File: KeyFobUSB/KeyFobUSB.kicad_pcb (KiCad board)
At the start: 2 copper layers, 54.3 x 18 mm, 17 parts, among them J1 USB_A, SW2 SW_SPDT, U1 ATtiny85V-10S

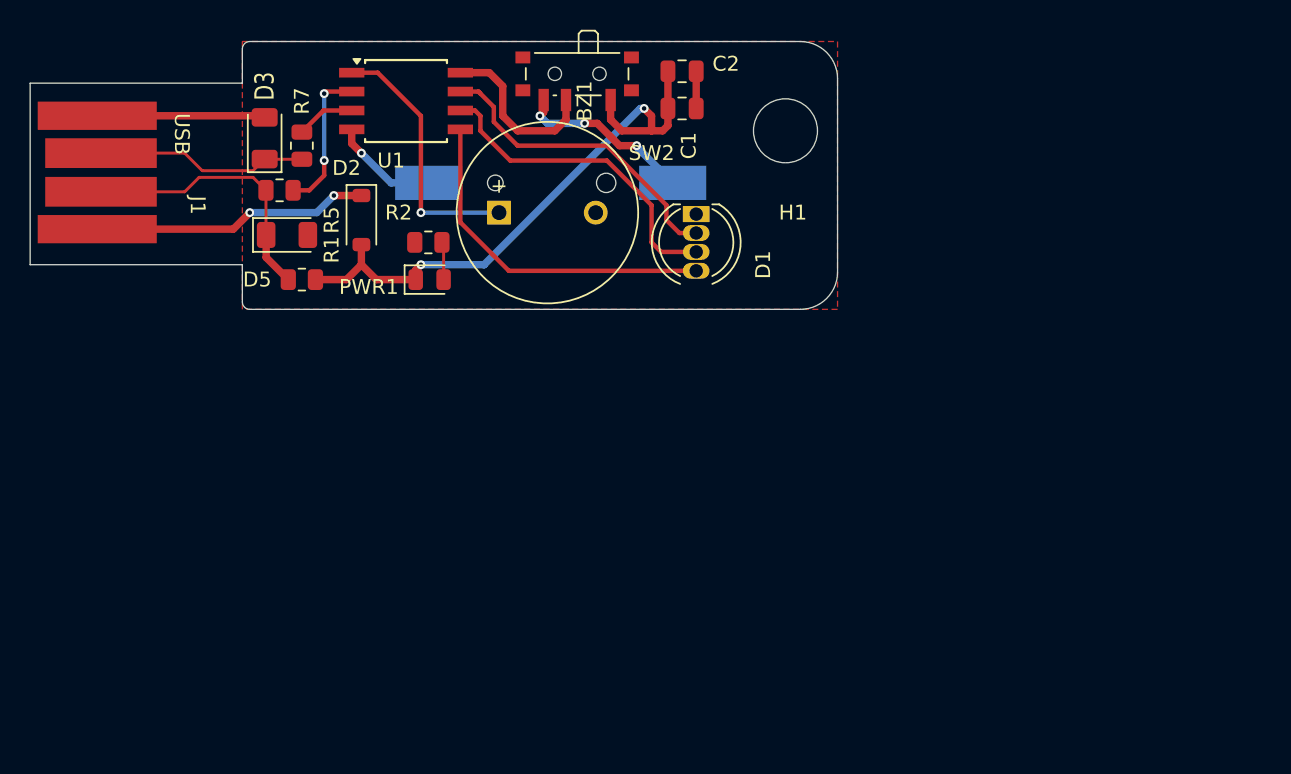
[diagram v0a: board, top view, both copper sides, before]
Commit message: Completed the schematic and placed the components on pcb
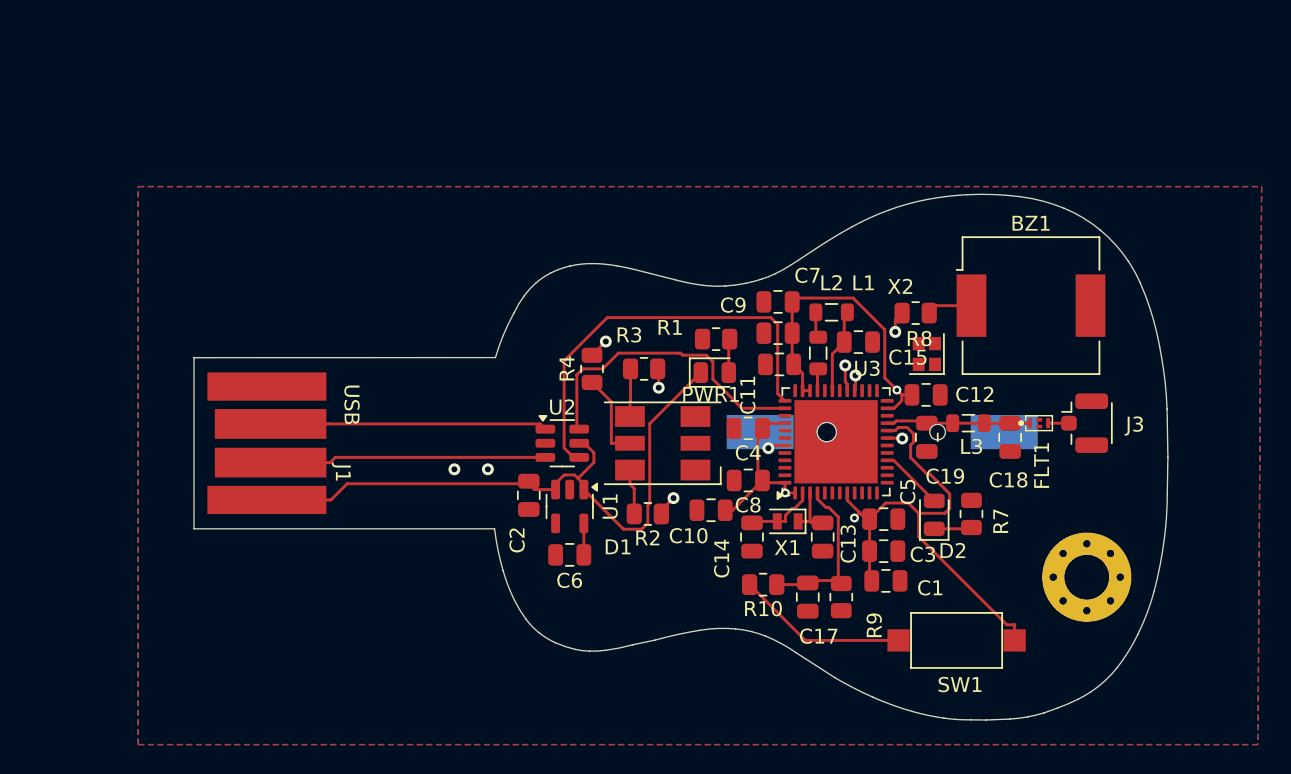
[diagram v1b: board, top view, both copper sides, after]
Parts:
- removed BT1: Battery_Cell, 22BatteryHoldercoincell_S8411-45R:S8411-45R_1
- removed D3, D5: 3.6V, Diode_SMD:D_1206_3216Metric
- removed H1: MountingHole, MountingHole:MountingHole_4.3mm_M4
- removed R5: 68, Resistor_SMD:R_0805_2012Metric
- removed SW2: SW_SPDT, Button_Switch_SMD:SW_SPDT_PCM12
- added C10: 100n, Capacitor_SMD:C_0805_2012Metric, F.Cu at (133.5, 79.5)
- added C11: 100n, Capacitor_SMD:C_0805_2012Metric, F.Cu at (138.1, 69.7)
- added C12: 100n, Capacitor_SMD:C_0805_2012Metric, F.Cu at (147.9, 71.8)
- added C13: 10p, Capacitor_SMD:C_0805_2012Metric, F.Cu at (141.0, 81.3)
- added C14: 10p, Capacitor_SMD:C_0805_2012Metric, F.Cu at (136.2, 81.3)
- added C15: 4u7, Capacitor_SMD:C_0805_2012Metric, F.Cu at (143.4, 68.2)
- added C17: 100n, Capacitor_SMD:C_0805_2012Metric, F.Cu at (140.0, 85.3)
- added C18: 0p8, Capacitor_SMD:C_0805_2012Metric, F.Cu at (153.6, 74.6)
- added C19: 0p8, Capacitor_SMD:C_0805_2012Metric, F.Cu at (148.0, 74.6)
- added C3: 100n, Capacitor_SMD:C_0805_2012Metric, F.Cu at (145.1, 82.2)
- added C4: 100n, Capacitor_SMD:C_0805_2012Metric, F.Cu at (136.0, 74.0)
- added C5: 100n, Capacitor_SMD:C_0805_2012Metric, F.Cu at (145.1, 80.1)
- added C6: 4u7, Capacitor_SMD:C_0805_2012Metric, F.Cu at (124.0, 82.5)
- added C7: 100n, Capacitor_SMD:C_0805_2012Metric, F.Cu at (138.0, 67.6)
- added C8: 100n, Capacitor_SMD:C_0805_2012Metric, F.Cu at (136.0, 77.5)
- added C9: 4u7, Capacitor_SMD:C_0805_2012Metric, F.Cu at (138.0, 65.5)
- added FLT1: DLF162500LT-5028A1, DLF162500LT-5028A1:DLF162500LT-5028A1, F.Cu at (155.5, 73.7)
- added H+1: MountingHole_Pad, MountingHole:MountingHole_3mm_Pad_Via, F.Cu at (158.8, 84.0)
- added J2: S8411-45R, 22BatteryHoldercoincell_S8411-45R:S8411-45R_1, B.Cu at (145.0, 74.2)
- added J3: Conn_Coaxial, Connector_Coaxial:U.FL_Hirose_U.FL-R-SMT-1_Vertical, F.Cu at (158.6, 73.7)
- added L1: 10n, Inductor_SMD:L_0805_2012Metric, F.Cu at (140.7, 68.9)
- added L2: 10u, Inductor_SMD:L_0805_2012Metric, F.Cu at (141.6, 66.2)
- added L3: 2n7, Inductor_SMD:L_0805_2012Metric, F.Cu at (150.8, 73.7)
- added R10: 220, Resistor_SMD:R_0805_2012Metric, F.Cu at (137.0, 84.5)
- added R3: 220, Resistor_SMD:R_0805_2012Metric, F.Cu at (129.0, 70.0)
- added R4: 220, Resistor_SMD:R_0805_2012Metric, F.Cu at (125.5, 70.0)
- added R8: 220, Resistor_SMD:R_0805_2012Metric, F.Cu at (147.2, 66.2)
- added R9: 5k1, Resistor_SMD:R_0805_2012Metric, F.Cu at (142.2, 85.3)
- added SW1: SW_Push, Button_Switch_SMD:SW_SPST_CK_RS282G05A3, F.Cu at (150.0, 88.2)
- added U2: USBLC6-2SC6, Package_TO_SOT_SMD:SOT-23-6, F.Cu at (123.5, 75.0)
- added U3: STM32WB55CEU6, Package_DFN_QFN:QFN-48-1EP_7x7mm_P0.5mm_EP5.6x5.6mm, F.Cu at (141.9, 74.9)
- added X1: 32kHz768, Crystal:Crystal_SMD_2012-2Pin_2.0x1.2mm, F.Cu at (138.7, 80.2)
- added X2: 32MHz, Crystal:Crystal_SMD_2016-4Pin_2.0x1.6mm, F.Cu at (148.0, 69.0)
- BZ1: footprint Buzzer_Beeper:MagneticBuzzer_ProSignal_ABT-410-RC -> Buzzer_Beeper:Buzzer_CUI_CPT-9019S-SMT
- C1: value 4.7uF -> 4u7
- C2: value 0.1uF -> 4u7
- D1: value LED_KRGB -> LED_RGB; footprint LED_THT:LED_D5.0mm-4_RGB -> LED_SMD:LED_Inolux_IN-P55TATRGB_PLCC6_5.0x5.5mm_P1.8mm
- D2: value MBR0520LT -> LED; footprint Diode_SMD:D_SOD-123 -> LED_SMD:LED_0805_2012Metric
- R1: value 1K5 -> 1K
- R2: value 1K -> 220
- R7: value 68 -> 220
- U1: value ATtiny85V-10S -> MIC5365-3.3YD5; footprint Package_SO:SOIC-8W_5.3x5.3mm_P1.27mm -> Package_TO_SOT_SMD:SOT-23-5
- moved R7 51.4 mm to (151.0, 79.8)
- moved D2 43.3 mm to (148.5, 79.8), turned to 90 degrees
- moved BZ1 36.3 mm to (155.0, 65.8)
- moved C1 34.6 mm to (145.2, 84.2)
- moved C2 30.3 mm to (121.2, 78.5), turned to -90 degrees
- moved U1 29.4 mm to (124.0, 79.2), turned to -90 degrees
- moved R1 28.1 mm to (133.8, 68.0)
- moved R2 23.5 mm to (129.2, 79.8)
- moved J1 21.5 mm to (98.8, 75.0)
- moved PWR1 20.2 mm to (133.8, 70.2)
- moved D1 15.6 mm to (130.2, 75.0), turned to 180 degrees
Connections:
- BZ1 pad 1: /Buzzer -> Net-(BZ1-+)
- C1 pad 1: +5V -> +3.3V
- D1 pad 2: /Red -> GND
- D1 pad 3: /Green -> GND
- D1 pad 4: /Blue -> Net-(D1-BA)
- D2 pad 1: Net-(D2-K) -> /LED_K
- D2 pad 2: +5V -> /LED_A
- J1 pad 1: Net-(D2-K) -> +5V
- J1 pad 2: /D- -> Net-(J1-D-)
- J1 pad 3: /D+ -> Net-(J1-D+)
- R1 pad 1: +5V -> Net-(PWR1-A)
- R1 pad 2: /D- -> GND
- R2 pad 1: Net-(PWR1-A) -> Net-(U3-PB0)
- R2 pad 2: GND -> Net-(D1-RA)
- R7 pad 1: /PB4 -> GND
- R7 pad 2: /D+ -> /LED_K
- U1 pad 1: /Buzzer -> +5V
- U1 pad 2: /PB3 -> GND
- U1 pad 3: /PB4 -> +5V
- U1 pad 4: GND -> unconnected-(U1-NC-Pad4)
- U1 pad 5: /Blue -> Net-(U1-VOUT)
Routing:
- net +3.3V: track 0.00 -> 80.3 mm, vias 0 -> 3
- net /USB_D-: track 0.00 -> 28.2 mm
- net /Blue: track 23.4 -> 0.00 mm
- net /Green: track 21.8 -> 0.00 mm
- net GND: track 21.5 -> 0.00 mm, vias 1 -> 2
- net /Red: track 21.1 -> 0.00 mm
- net /USB_D+: track 0.00 -> 20.5 mm
- net Net-(U3-PB2): track 0.00 -> 20.1 mm, vias 0 -> 2
- net Net-(U3-PB1): track 0.00 -> 19.8 mm, vias 0 -> 2
- net Net-(D2-K): track 18.7 -> 0.00 mm, vias 2 -> 0
- net Net-(J1-D-): track 0.00 -> 18.6 mm
- net Net-(J1-D+): track 0.00 -> 18.6 mm
- net /D-: track 18.5 -> 0.00 mm
- net Net-(U3-PB0): track 0.00 -> 18.1 mm, vias 0 -> 2
- net /Buzzer: track 17.6 -> 0.00 mm, vias 1 -> 0
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- added copper zone on B.Cu, net GND
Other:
- board size 54.3 x 18 mm -> 65.5 x 35.3 mm
- copper layers 2 -> 4
- rule pad_to_mask_clearance: 0 -> 0.08

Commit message: added battery holder and vias
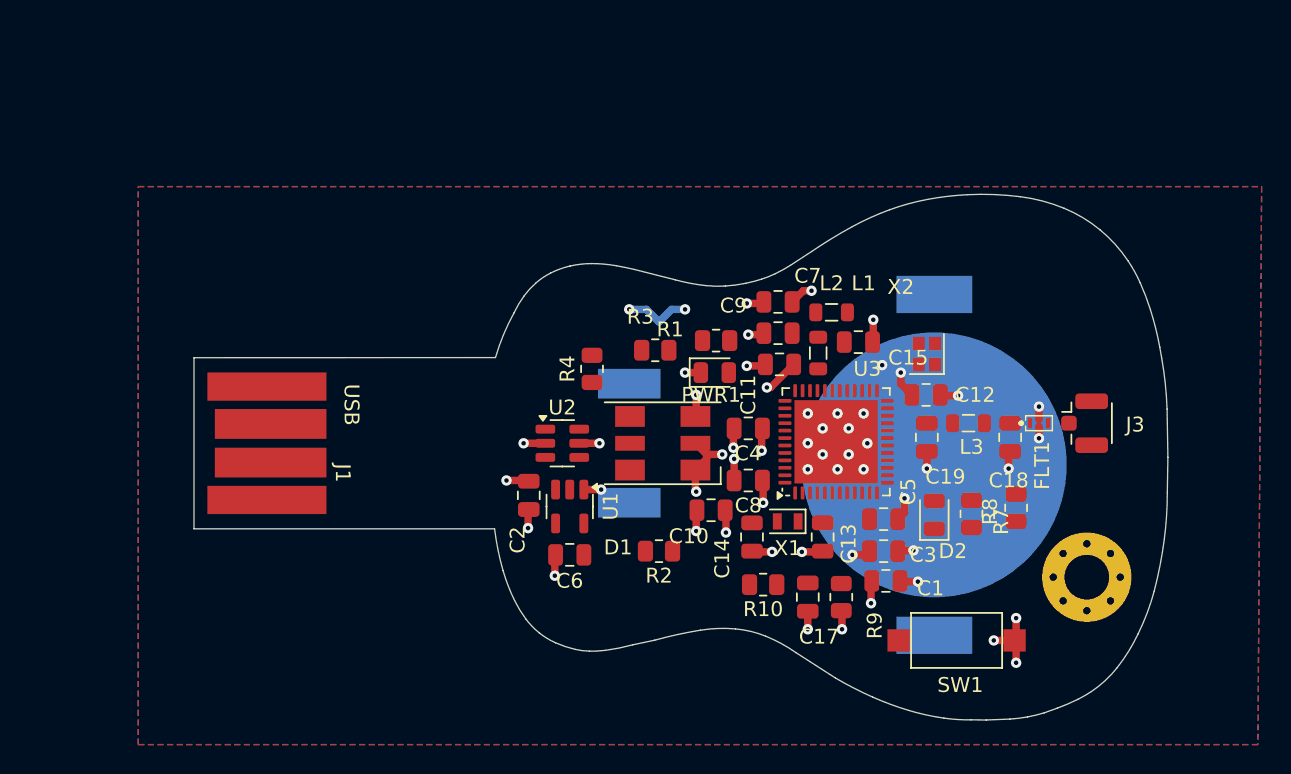
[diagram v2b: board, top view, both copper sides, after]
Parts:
- removed J2: S8411-45R, 22BatteryHoldercoincell_S8411-45R:S8411-45R_1
- added BT1: BAT-HLD-001, 22BatteryHoldercoincell_S8411-45R:BATHLD001 CR2032, B.Cu at (148.5, 76.5)
- BZ1: moved to B.Cu
- moved BZ1 28.5 mm to (128.0, 75.0), turned to 90 degrees
- moved R8 14.7 mm to (154.0, 79.3), turned to 90 degrees
- moved R2 2.61 mm to (130.0, 82.2)
- moved R3 1.46 mm to (129.8, 68.8)
- moved R1 0.10 mm to (133.8, 68.1)
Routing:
- net +3.3V: track 80.3 -> 17.7 mm, vias 3 -> 11
- net GND: track 0.00 -> 42.2 mm, vias 2 -> 40
- net +5V: track 43.9 -> 5.11 mm, vias 0 -> 4
- net /USB_D-: track 28.2 -> 0.00 mm
- net /USB_D+: track 20.5 -> 0.00 mm
- net Net-(U3-PB2): track 20.1 -> 0.00 mm, vias 2 -> 0
- net Net-(U3-PB1): track 19.8 -> 0.00 mm, vias 2 -> 0
- net Net-(J1-D-): track 18.6 -> 0.00 mm
- net Net-(J1-D+): track 18.6 -> 0.00 mm
- net Net-(U3-PB0): track 18.1 -> 0.00 mm, vias 2 -> 0
- net Net-(U3-PB3): track 15.1 -> 0.00 mm, vias 2 -> 0
- net Net-(R10-Pad2): track 11.6 -> 0.00 mm
- net /BOOT0: track 11.1 -> 0.00 mm
- net /RF: track 9.71 -> 0.00 mm
- net Net-(D1-GA): track 5.88 -> 0.00 mm
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- added copper zone on In1.Cu, net GND
- added copper zone on In2.Cu, net GND

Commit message: Added the PCB image
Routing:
- net GND: track 42.2 -> 37.8 mm, vias 40 -> 38
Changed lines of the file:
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@@
 		(layer "Edge.Cuts")
-	)
-	(dimension
-		(type aligned)
-		(layer "B.Cu")
-		(pts
-			(xy 160 65) (xy 160 78)
-		)
-		(height -18)
-		(gr_text "0.5118 in"
-			(at 176.2 71.5 90)
-			(layer "B.Cu")
-			(effects
-				(font
-					(size 1.5 1.5)
-					(thickness 0.3)
-				)
-			)
-		)
-		(format
-			(prefix "")
-			(suffix "")
-			(units 3)
-			(units_format 1)
-			(precision 4)
-		)
-		(style
-			(thickness 0.2)
-			(arrow_length 1.27)
-			(text_position_mode 0)
-			(extension_height 0.58642)
-			(extension_offset 0.5) keep_text_aligned)
 	)
 	(segment
@@
 	)
 	(via
-		(at 131.75 66)
-		(size 0.7)
-		(drill 0.3)
-		(layers "F.Cu" "B.Cu")
-		(free yes)
-		(net 2)
-	)
-	(via
 		(at 139.6 82.3)
 		(size 0.7)
@@
 	(via
 		(at 155.5375 72.5375)
-		(size 0.7)
-		(drill 0.3)
-		(layers "F.Cu" "B.Cu")
-		(free yes)
-		(net 2)
-	)
-	(via
-		(at 128 66)
 		(size 0.7)
 		(drill 0.3)
@@
 		(width 0.5)
 		(layer "B.Cu")
-		(net 2)
-	)
-	(segment
-		(start 128 66)
-		(end 129.15 66)
-		(width 0.5)
-		(layer "B.Cu")
-		(net 2)
-	)
-	(segment
-		(start 129.15 66)
-		(end 130 66.85)
-		(width 0.5)
-		(layer "B.Cu")
-		(net 2)
-	)
-	(segment
-		(start 130.85 66)
-		(end 130 66.85)
-		(width 0.5)
-		(layer "B.Cu")
-		(net 2)
-	)
-	(segment
-		(start 131.75 66)
-		(end 130.85 66)
-		(width 0.5)
-		(layer "B.Cu")

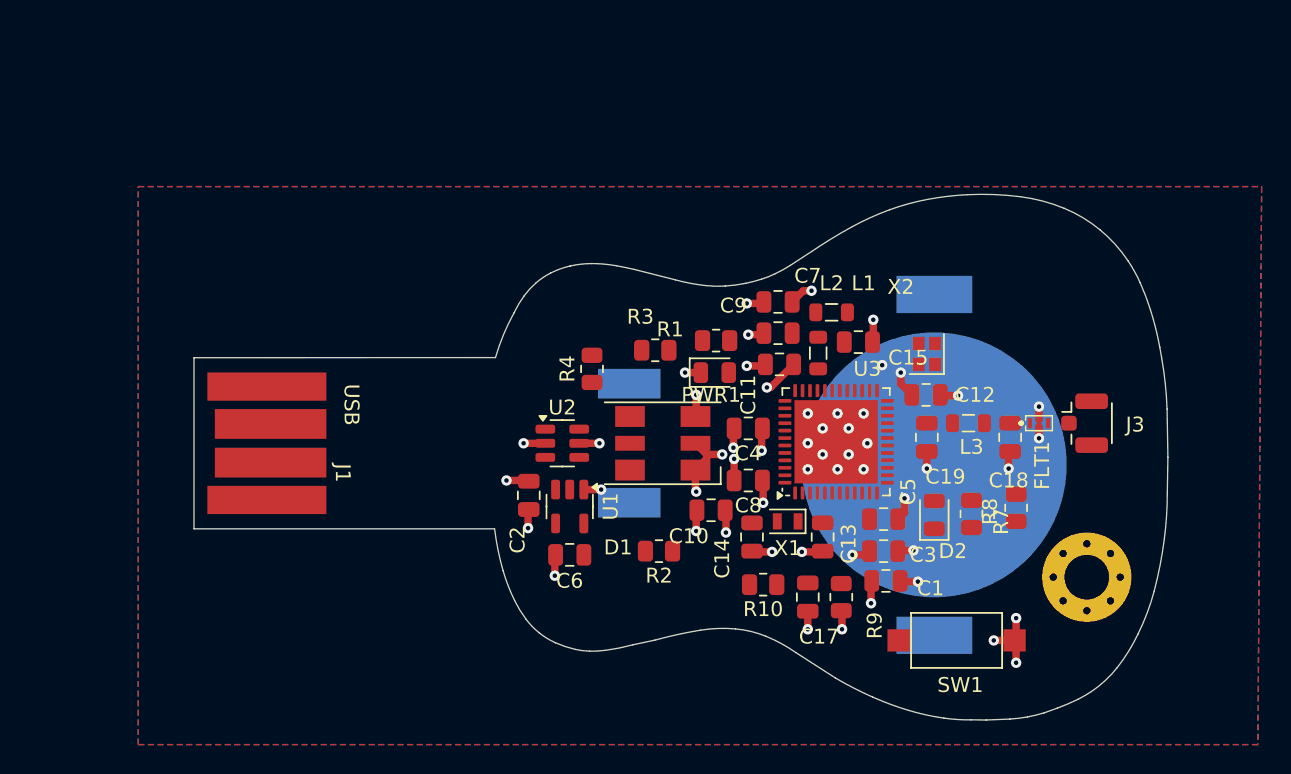
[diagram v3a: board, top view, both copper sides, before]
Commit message: Added the Bluetooth SMD Antenna and marked the area.
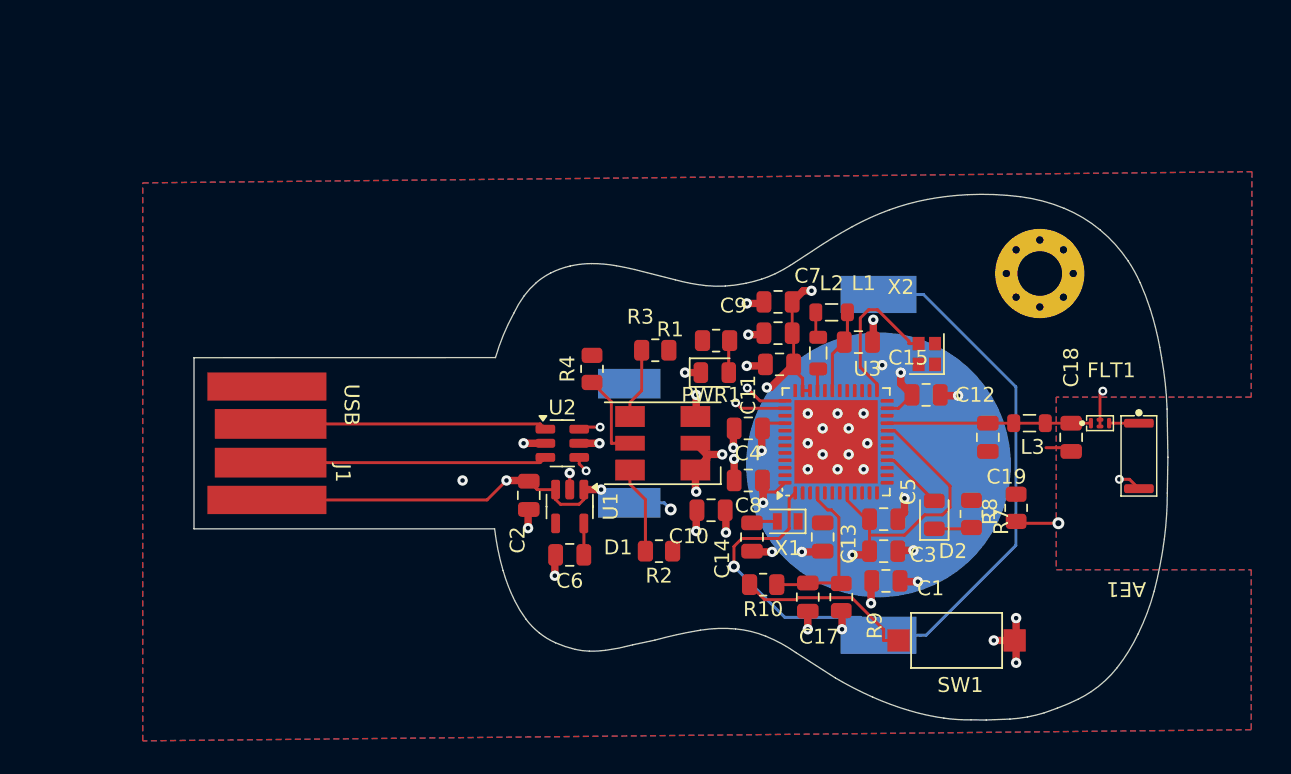
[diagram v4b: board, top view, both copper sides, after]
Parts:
- removed J3: Conn_Coaxial, Connector_Coaxial:U.FL_Hirose_U.FL-R-SMT-1_Vertical
- added AE1: Antenna_Chip, RF Ceramic Antenna QJ-13799-2-2019:RF Ceramic Antenna QJ-13799-2-2019, F.Cu at (162.2, 75.8)
- moved H+1 20.7 mm to (155.6, 63.6)
- moved C18 4.10 mm to (157.7, 74.6)
- moved C19 4.10 mm to (152.1, 74.6)
- moved FLT1 4.10 mm to (159.6, 73.7)
- moved L3 4.10 mm to (154.9, 73.7)
- moved BT1 3.75 mm to (144.8, 76.5)
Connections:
- net Net-(J1-D+) renamed /USBC_D+
- net Net-(J1-D-) renamed /USBC_D-
- U2 pad 4: /USB_D- -> /USB_D+
- U2 pad 6: /USB_D+ -> /USB_D-
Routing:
- net +3.3V: track 17.7 -> 87.9 mm
- net /VBAT: track 0.00 -> 53.9 mm, vias 0 -> 1
- net +5V: track 5.11 -> 38.2 mm
- net Net-(BZ1-+): track 0.00 -> 32.3 mm, vias 0 -> 2
- net /USB_D-: track 0.00 -> 19.1 mm, vias 0 -> 2
- net /USBC_D-: track 0.00 -> 18.6 mm
- net /USBC_D+: track 0.00 -> 18.6 mm
- net /USB_D+: track 0.00 -> 16.5 mm, vias 0 -> 2
- net /RF: track 0.00 -> 13.7 mm
- net Net-(R10-Pad2): track 0.00 -> 12.1 mm
- net /BOOT0: track 0.00 -> 11.2 mm
- net /HSC_IN: track 0.00 -> 10.5 mm
- net GND: track 37.8 -> 46.0 mm
- net Net-(D1-RA): track 0.00 -> 5.88 mm
- net Net-(D1-GA): track 0.00 -> 5.88 mm
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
